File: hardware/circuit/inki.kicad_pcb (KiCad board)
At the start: 2 copper layers, 47.2 x 55.5 mm, 49 parts, among them J1 connector epaper, J2 Conn_01x02_Socket, J3 Conn_01x02_Socket, J4 Conn_01x02_Socket, J5 Conn_01x02_Socket, J7 Conn_01x02_Socket, Q1 TSM260P02CX, Q2 MMBT3904, Q3 IRLML6344TRPBF, SW1 SW_DIP_x04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

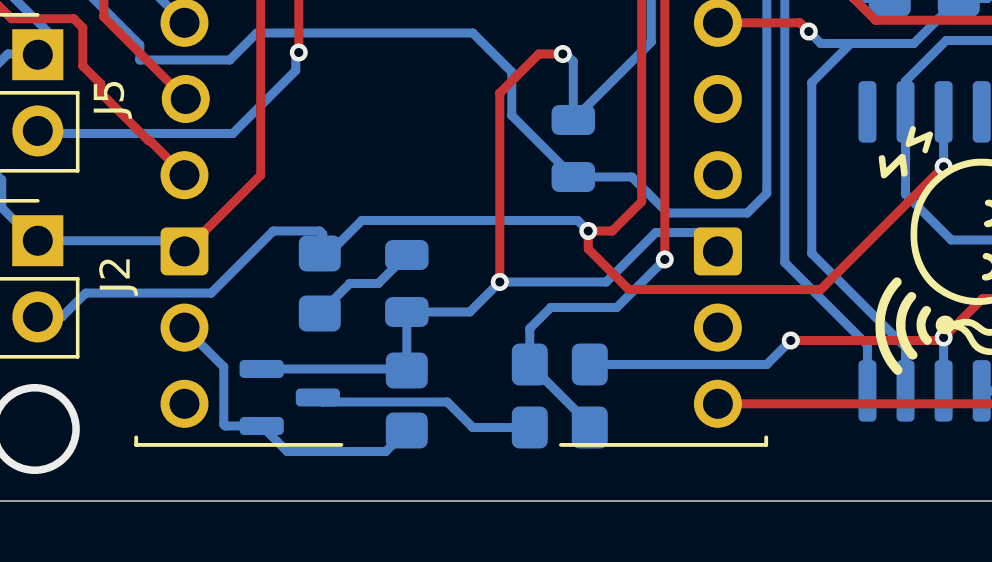
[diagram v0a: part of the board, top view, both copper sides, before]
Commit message: hardware: gate VBAT divider with PFET to stop leakage in off-state
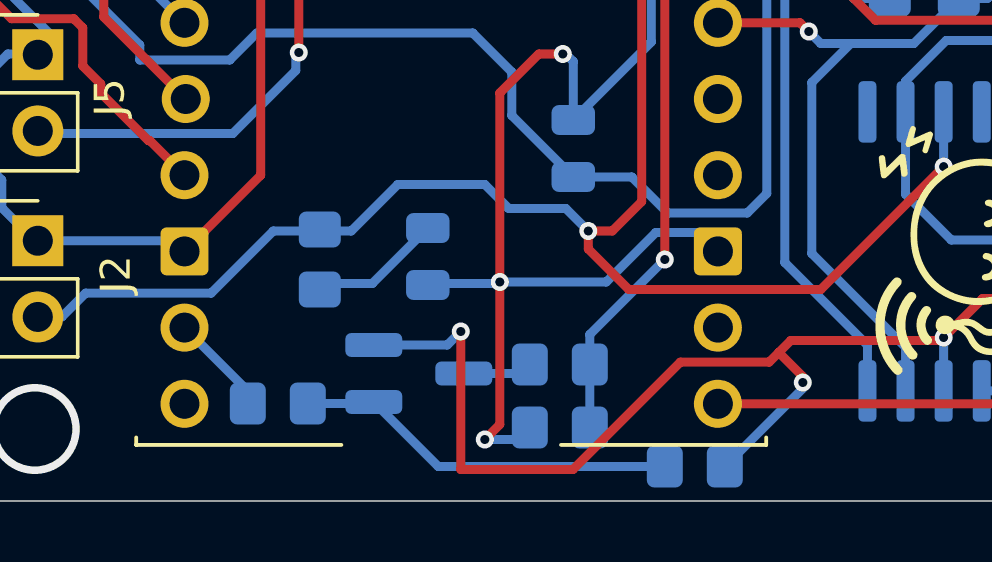
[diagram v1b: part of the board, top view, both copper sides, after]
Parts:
- added R21: 100k, Resistor_SMD:R_0805_2012Metric_Pad1.20x1.40mm_HandSolder, B.Cu at (26.0, 66.9)
- Q3: value IRLML6344TRPBF -> TSM260P02CX; footprint Package_TO_SOT_SMD:SOT-23 -> Package_TO_SOT_SMD:SOT-23_Handsoldering
- moved R15 9.85 mm to (39.9, 69.0), turned to 180 degrees
- moved Q3 4.37 mm to (30.7, 65.9)
- moved 100n1 1.14 mm to (31.0, 62.0)
- moved R10 0.80 mm to (27.4, 62.1)
- turned R1 to 0 degrees
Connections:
- Q3 pad 2: GND -> Net-(D1-K)
- R1 pad 1: Net-(D1-K) -> Net-(Q3-D)
- R14 pad 2: Net-(Q3-D) -> GND
- R15 pad 1: Net-(Q3-G) -> Net-(D1-K)
- R15 pad 2: GND -> Net-(Q3-G)
- pico1 pad 19: Net-(Q3-G) -> Net-(pico1-GP14)
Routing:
- net Net-(D1-K): track 35.5 -> 54.2 mm, vias 3 -> 4
- net Net-(Q3-D): track 7.48 -> 2.32 mm
- net Net-(pico1-GP14): track 0.00 -> 3.40 mm
- net Net-(pico1-GP27): track 33.4 -> 30.5 mm
- net Net-(Q3-G): track 10.5 -> 12.8 mm
- net GND: track 275.3 -> 274.5 mm, vias 7 -> 8
- net Net-(100n1-Pad1): track 3.71 -> 4.45 mm
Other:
- board text removed: "6344"

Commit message: improved coin cell voltage measurement
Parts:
- added Q4: MMBT3904, Package_TO_SOT_SMD:SOT-23, B.Cu at (26.2, 66.2)
- added R22: 50k, Resistor_SMD:R_0805_2012Metric_Pad1.20x1.40mm_HandSolder, B.Cu at (20.5, 65.4)
- R15: value 1M -> 2.2M
- R21: value 100k -> 1k
- moved R21 4.36 mm to (26.7, 62.6), turned to 0 degrees
- moved R10 2.60 mm to (27.3, 59.5)
- moved 100n1 2.56 mm to (30.1, 59.6), turned to 90 degrees
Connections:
- R21 pad 1: Net-(Q3-G) -> Net-(pico1-GP14)
- R21 pad 2: Net-(pico1-GP14) -> Net-(Q4-B)
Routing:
- net GND: track 274.5 -> 293.8 mm, vias 8 -> 10
- net Net-(J2-Pin_2): track 106.1 -> 110.8 mm
- net Net-(Q4-B): track 0.00 -> 3.68 mm
- net Net-(pico1-GP14): track 3.40 -> 5.95 mm
- net Net-(100n1-Pad1): track 4.45 -> 2.82 mm
- net Net-(Q3-G): track 12.8 -> 13.7 mm

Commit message: updated pcb, unified part names, added BOM
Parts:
- C1, C3: value C_Small -> 100nF
- C2: renamed from 100n1; value C_Small -> 100nF
- C4: renamed from 100n2; value C_Small -> 100nF
- C5: renamed from 100n3; value C_Small -> 100nF
- C6: renamed from 100n5; value C_Small -> 100nF
- C7: renamed from 100n4; value C_Small -> 100nF

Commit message: add optional i2c sensor sheet and align bom values
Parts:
- R15: value 2.2M -> 2M2
- R16: value 22 -> 22R
- R3, R4: value 4.7k -> 4k7
- R6: value 220 R -> 220R
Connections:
- net Net-(J1-Pin_8) renamed 3V3
- net Net-(U1-SCL) renamed /optional i2c device/SCL
- net Net-(U1-SDA) renamed /optional i2c device/SDA

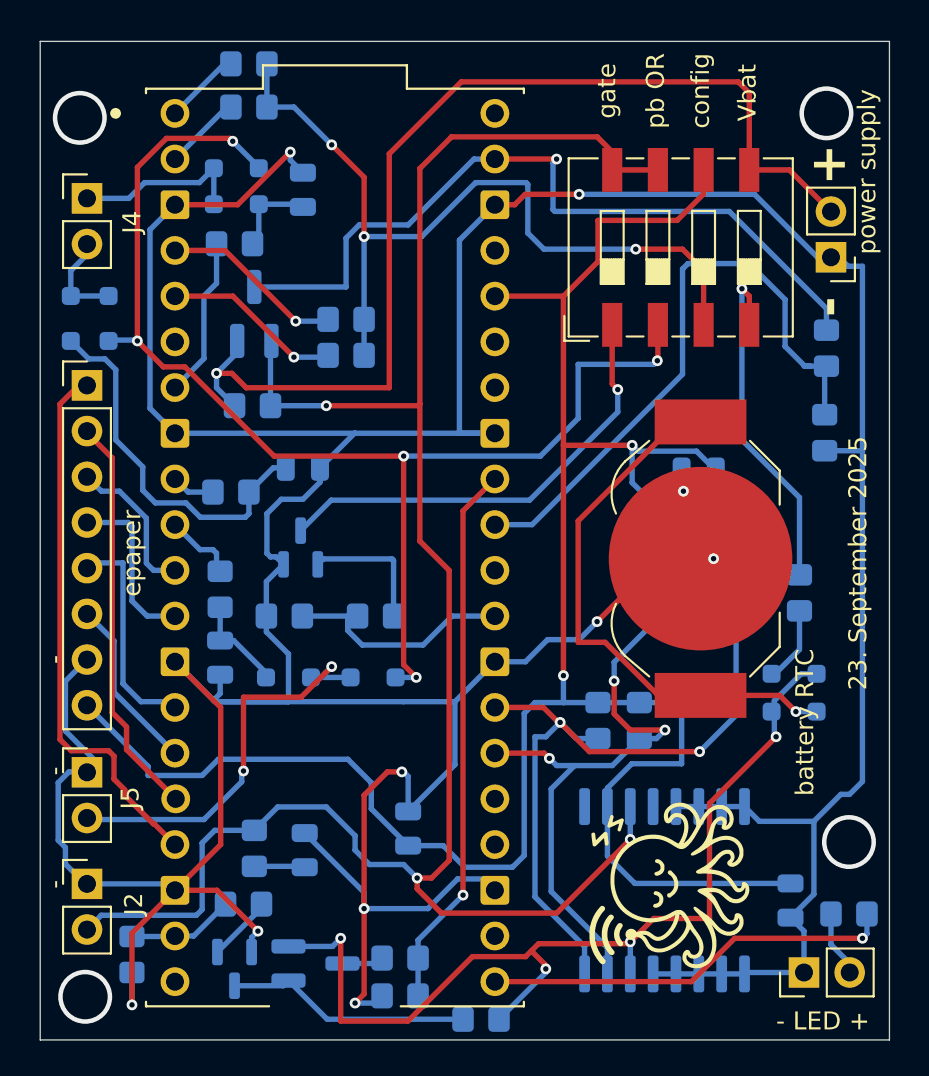
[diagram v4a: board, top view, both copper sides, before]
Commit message: added optional i2c device, added gerber files - not tested! Use with care!
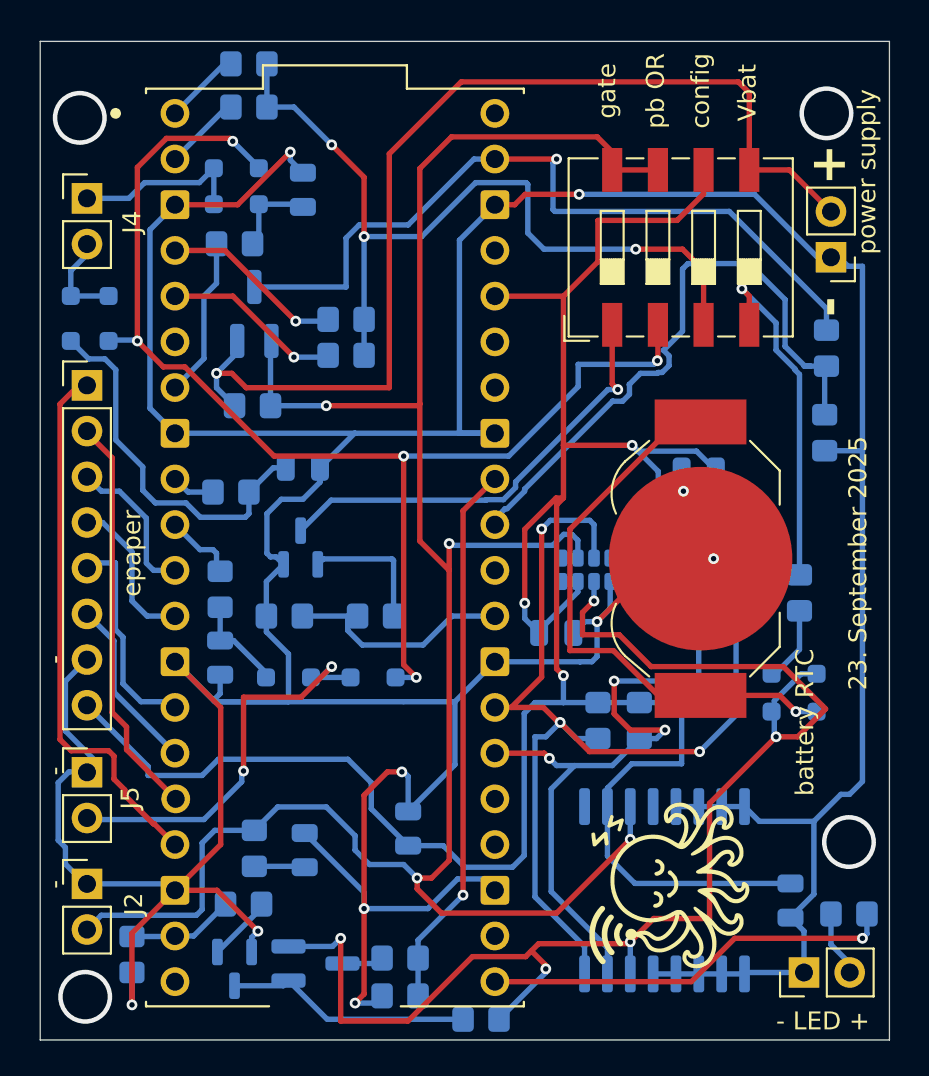
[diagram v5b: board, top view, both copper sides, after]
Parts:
- added C8: 100nF, Capacitor_SMD:C_0805_2012Metric, B.Cu at (44.1, 47.5)
- added U3: RV-3028-C7, Package_SON:MicroCrystal_C7_SON-8_1.5x3.2mm_P0.9mm, B.Cu at (45.7, 44.0)
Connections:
- net /optional i2c device/SCL renamed /optional i2c devices/SCL
- net /optional i2c device/SDA renamed /optional i2c devices/SDA
- net Net-(D1-K) renamed Vbat
- net Net-(J2-Pin_2) renamed INT
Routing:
- net Vbat: track 54.2 -> 76.0 mm, vias 4 -> 5
- net /optional i2c devices/SCL: track 45.3 -> 61.0 mm, vias 2 -> 3
- net 3V3: track 127.8 -> 140.9 mm, vias 2 -> 3
- net INT: track 110.8 -> 120.8 mm, vias 3 -> 4
- net /optional i2c devices/SDA: track 39.0 -> 46.7 mm
- net GND: track 293.8 -> 299.0 mm
- net Net-(D4-A): track 70.7 -> 69.6 mm
- net Net-(D1-A): track 30.5 -> 31.4 mm
- net Net-(J1-Pin_4): track 9.48 -> 8.64 mm
- net Net-(Q2-C): track 25.4 -> 24.9 mm

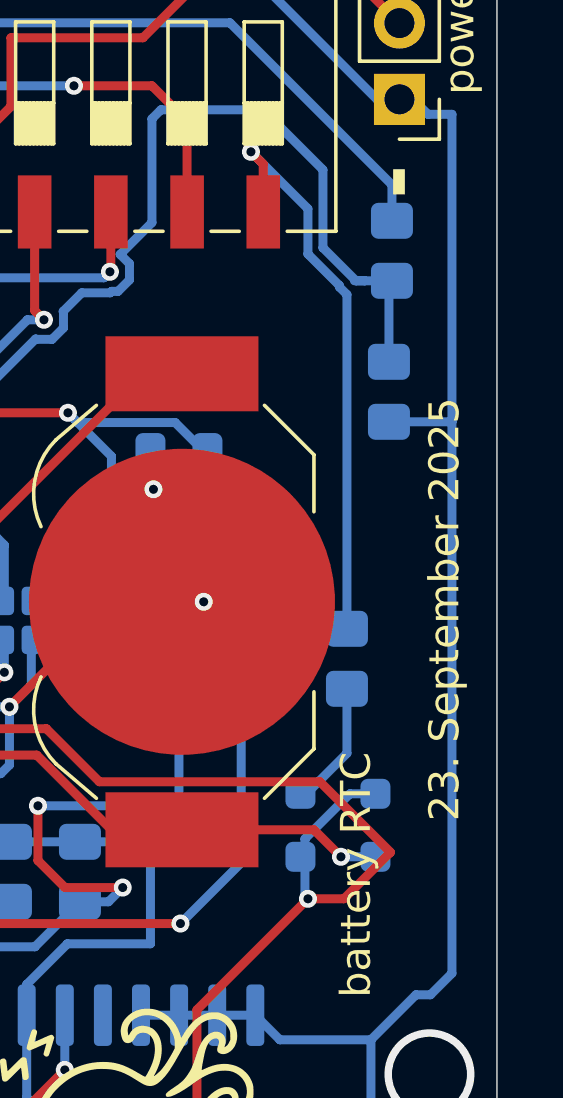
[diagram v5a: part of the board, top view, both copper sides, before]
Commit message: pcb edit - silk screen
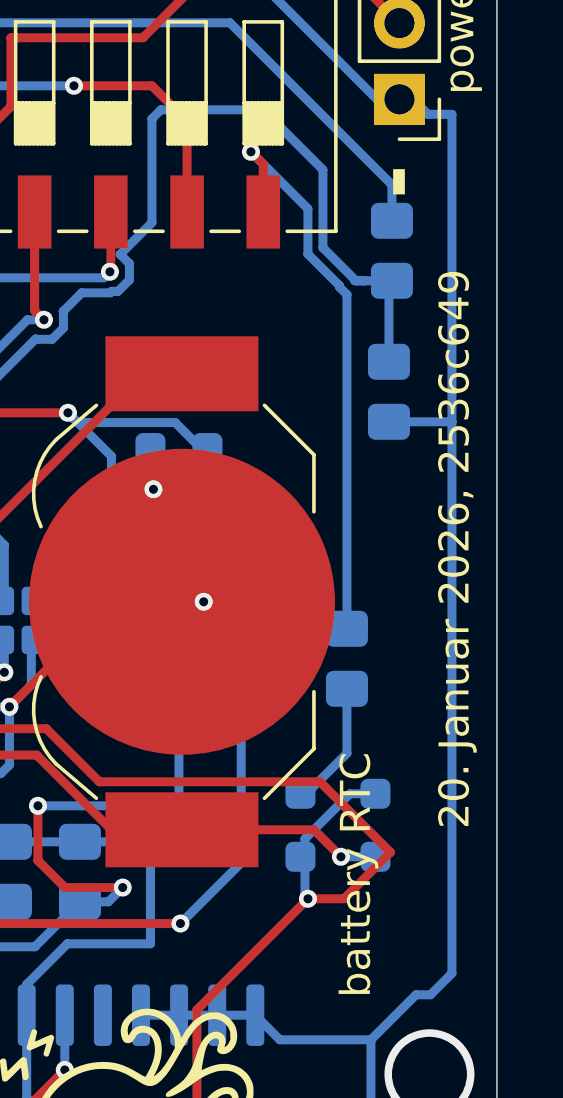
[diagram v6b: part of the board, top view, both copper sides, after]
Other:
- board text added: "20. Januar 2026, 2536c649"
- board text removed: "23. September 2025"
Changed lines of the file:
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@@
 		)
 	)
-	(gr_text "23. September 2025"
-		(at 60.85 43.65 90)
+	(gr_text "20. Januar 2026, 2536c649"
+		(at 61.19 41.64 90)
 		(layer "F.SilkS")
 		(effects
